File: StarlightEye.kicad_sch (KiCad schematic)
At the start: 96 parts, among them J1 QWIIC_CONNECTORJS-1MM, J2 FH12A-22S-0.5SH(55), J3 Conn_Coaxial, J4 Conn_Coaxial, J5 Conn_Coaxial, Q1 DMG2302UK-7, Q2 DMG2302UK-7, U1 AP3418KTR-G1, U2 LP5907MFX-1.8, U3 AP2161W, U4 IMX585, U5 ECS-2520MV-240-DN-TR

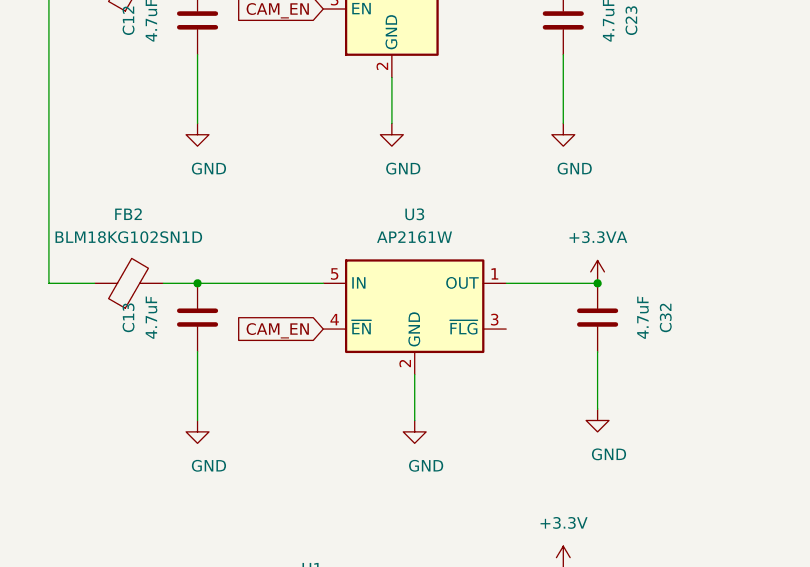
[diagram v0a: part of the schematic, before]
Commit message: Bug fix: swaping part no AP2161W with AP2171W to have the correct EN polarity
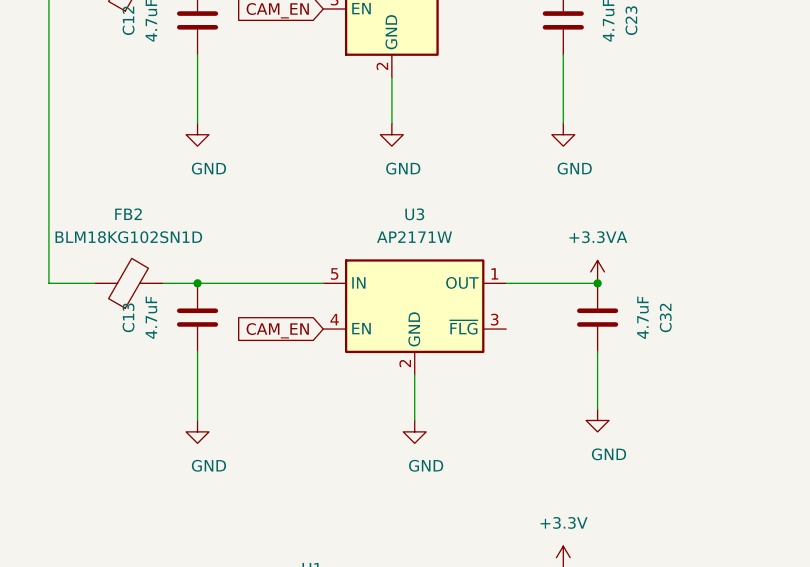
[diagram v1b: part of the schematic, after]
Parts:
- removed U3: AP2161W, Package_TO_SOT_SMD:SOT-23-5, symbol Power_Management:AP2161W
- added U3: AP2171W, Package_TO_SOT_SMD:SOT-23-5, symbol Power_Management:AP2171W
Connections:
- net +3.3VA: now also U3.1 (OUT)
- net CAM_EN: now also U3.4 (EN)
- net GND: now also U3.2 (GND)
- net at C13.2, FB2.2: now also U3.5 (IN)
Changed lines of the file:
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@@
     (pin "1")
+  )
+  (symbol (lib_id "Power_Management:AP2171W") (at 64.77 210.82 0) (unit 1)
+    (in_bom yes) (on_board yes) (fields_autoplaced)
+    (property "Reference" "U3" (id 0) (at 64.77 200.66 0))
+    (property "Value" "AP2171W" (id 1) (at 64.77 203.2 0))
+    (property "Footprint" "Package_TO_SOT_SMD:SOT-23-5" (id 2) (at 64.77 220.98 0)
+      (effects (font (size 1.27 1.27)) hide)
+    )
+    (property "Datasheet" "https://www.diodes.com/assets/Datasheets/AP2161.pdf" (id 3) (at 64.77 209.55 0)
+      (effects (font (size 1.27 1.27)) hide)
+    )
+    (pin "1")
+    (pin "2")
+    (pin "3")
+    (pin "4")
+    (pin "5")
   )
   (symbol (lib_id "power:+1V1") (at 92.71 107.95 0) (unit 1)
@@
     (pin "1")
     (pin "2")
-  )
-  (symbol (lib_id "Power_Management:AP2161W") (at 64.77 210.82 0) (unit 1)
-    (in_bom yes) (on_board yes) (fields_autoplaced)
-    (property "Reference" "U3" (id 0) (at 64.77 200.66 0))
-    (property "Value" "AP2161W" (id 1) (at 64.77 203.2 0))
-    (property "Footprint" "Package_TO_SOT_SMD:SOT-23-5" (id 2) (at 64.77 220.98 0)
-      (effects (font (size 1.27 1.27)) hide)
-    )
-    (property "Datasheet" "https://www.diodes.com/assets/Datasheets/AP2161.pdf" (id 3) (at 64.77 209.55 0)
-      (effects (font (size 1.27 1.27)) hide)
-    )
-    (pin "1")
-    (pin "2")
-    (pin "3")
-    (pin "4")
-    (pin "5")
   )
   (symbol (lib_id "power:GND") (at 39.37 43.18 0) (unit 1)
@@
       (reference "U2") (unit 1) (value "LP5907MFX-1.8") (footprint "Package_TO_SOT_SMD:SOT-23-5")
     )
-    (path "/b70f92fc-e7da-4598-aac3-42894166b45e"
-      (reference "U3") (unit 1) (value "AP2161W") (footprint "Package_TO_SOT_SMD:SOT-23-5")
+    (path "/2c71736d-9bd1-425e-bf48-2682b064493a"
+      (reference "U3") (unit 1) (value "AP2171W") (footprint "Package_TO_SOT_SMD:SOT-23-5")
     )
     (path "/b928e7ba-db52-4d1a-8842-81747bfca67f"

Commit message: V1.6 init
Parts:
- removed C13: 4.7uF, Capacitor_SMD:C_0603_1608Metric, symbol Device:C
- removed FB1, FB2: BLM18KG102SN1D, Inductor_SMD:L_0603_1608Metric, symbol Device:FerriteBead
- removed J1: QWIIC_CONNECTORJS-1MM, Connector_JST:JST_SH_SM04B-SRSS-TB_1x04-1MP_P1.00mm_Horizontal, symbol SparkFun-Connectors:QWIIC_CONNECTORJS-1MM
- removed Q1, Q2: DMG2302UK-7, Package_TO_SOT_SMD:SOT-23, symbol Transistor_FET:DMN30H4D0L
- removed TP5: TestPoint, TestPoint:TestPoint_Pad_D1.0mm, symbol Connector:TestPoint
- removed U3: AP2171W, Package_TO_SOT_SMD:SOT-23-5, symbol Power_Management:AP2171W
- added C13, C60: C_Feedthrough, footprints:NFM18CC101R1C3D, symbol Device:C_Feedthrough
- added C48, C51, C52, C53, C54, C55, C56: 100nF, Capacitor_SMD:C_0402_1005Metric, symbol Device:C
- added C49, C57: 10nF, Capacitor_SMD:C_0402_1005Metric, symbol Device:C
- added C50: 10uF, Capacitor_SMD:C_0603_1608Metric, symbol Device:C
- added C58: 100pF, Capacitor_SMD:C_0402_1005Metric, symbol Device:C
- added C59: 4.7uF, Capacitor_SMD:C_0603_1608Metric, symbol Device:C
- added C61: 120pF, Capacitor_SMD:C_0402_1005Metric, symbol Device:C
- added C62: 22uF, Capacitor_SMD:C_0805_2012Metric, symbol Device:C
- added D1: MBR0540, Diode_SMD:D_SOD-123, symbol Diode:MBR0540
- added FB4: BLM18KG102SN1D, Inductor_SMD:L_0402_1005Metric, symbol Device:FerriteBead
- added J1: Conn_01x04_Shielded, Connector_JST:JST_SH_SM04B-SRSS-TB_1x04-1MP_P1.00mm_Horizontal, symbol Connector_Generic_Shielded:Conn_01x04_Shielded
- added J6: Conn_01x02_Shielded, Connector_Molex:Molex_PicoBlade_53398-0271_1x02-1MP_P1.25mm_Vertical, symbol Connector_Generic_Shielded:Conn_01x02_Shielded
- added J7: Conn_01x02_Shielded, Connector_Molex:Molex_PicoBlade_53261-0271_1x02-1MP_P1.25mm_Horizontal, symbol Connector_Generic_Shielded:Conn_01x02_Shielded
- added R11, R13: 10K, Resistor_SMD:R_0402_1005Metric, symbol Device:R
- added R12: 1.15K, Resistor_SMD:R_0402_1005Metric, symbol Device:R
- added R14: 2K, Resistor_SMD:R_0402_1005Metric, symbol Device:R
- added TP14, TP7, TP_3V1: TestPoint, TestPoint:TestPoint_Pad_D1.0mm, symbol Connector:TestPoint
- added U10: TVS0500DRV, Package_SON:WSON-6-1EP_2x2mm_P0.65mm_EP1x1.6mm, symbol Power_Protection:TVS0500DRV
- added U11: TPSM82821SILR, footprints:TPSM82821SILR, symbol TPSM82821SILR:TPSM82821SILR
- added U3: TPS7A90, Package_DFN_QFN:Texas_S-PDSO-N10_EP1.2x2mm, symbol Regulator_Linear:TPS7A90
- added U6: TMP117AIDRVR, footprints:TMP117AIDRVR, symbol 2021-03-21_22-07-02:TMP117AIDRVR
- added U7: STM8S003F3P, Package_SO:TSSOP-20_4.4x6.5mm_P0.65mm, symbol MCU_ST_STM8:STM8S003F3P
- added U8: DRV8837C, Package_SON:WSON-8-1EP_2x2mm_P0.5mm_EP0.9x1.6mm, symbol Driver_Motor:DRV8837C
- added U9: TCA9406DC, footprints:TCA9406DCUR, symbol Interface:TCA9406DC
- C32: value 4.7uF -> 10uF
- R6: value 1K -> 10K
- R7: value 1K -> 3.57K
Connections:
- net +1V1: now also C58.2
- net +1V8: now also JP1.1 (A), JP2.1 (A), C55.1, U9.3 (VCCA), U9.6 (OE); no longer R4.2, R5.1, R6.2, R7.1
- net +3.3VA: now also R7.2, C50.1, C57.2, U3.1 (OUT), U3.2 (OUT); no longer C32.1
- net +3V3: now also C51.1, C53.1, C56.1, FB4.1, J1.2 (Pin_2), U7.9 (VDD), U8.8 (VCC), U9.7 (VCCB); no longer FB3.2
- net ADDR0: now also R5.1; no longer R5.2
- net CAM_EN: now also R6.1, U3.7 (EN)
- net GND: now also J2.MP, R4.2, R5.2, R6.2, C13.2, C48.1, C49.2, C50.2, C51.2, C52.1, C53.2, C54.2, C55.2, C56.2, C59.1, C60.2, C62.2, J1.1 (Pin_1), J1.MP (Shield), J6.MP (Shield), J7.2 (Pin_2), J7.MP (Shield), R11.2, R12.1, R14.1, U10.1 (GND), U10.2 (GND), U10.3 (GND), U10.7 (GND), U11.10 (GND), U11.9 (GND), U3.11 (GND), U3.4 (GND), U6.2 (GND), U6.3 (ALERT), U6.4 (ADD0), U7.7 (VSS), U8.4 (GND), U8.9 (GND), U9.2 (GND); no longer JP1.1 (A), JP2.1 (A)
- net SCL_1V8: now also U9.5 (SCL_A); no longer R6.1
- net SCL_3V3: now also J1.4 (Pin_4), U6.1 (SCL), U7.12 (PC2), U9.8 (SCL_B)
- net SDA_1V8: now also U9.4 (SDA_A); no longer R7.2
- net SDA_3V3: now also J1.3 (Pin_3), U6.6 (SDA), U7.11 (PC1), U9.1 (SDA_B)
- net at C12.2, U2.1 (IN): now also C13.1, C61.1, C62.1, R13.2, TP_3V1.1, U11.5 (VOUT), U11.6 (VOUT), U11.7 (VOUT)
- net at R1.2, R2.1, U1.5 (FB): now also C58.1
- new net: C60.1, D1.1 (K), U10.4 (IN), U10.5 (IN), U10.6 (IN)
- new net: C61.2, R13.1, R14.2, U11.8 (FB)
- new net: C57.1, R12.2, R7.1, U3.3 (FB)
- new net: C49.1, U3.8 (NR/SS)
- new net: C48.2, FB4.2, U6.5 (V+)
- new net: C13.3, C32.1, U3.10 (IN), U3.6 (SS_CTRL), U3.9 (IN)
- new net: J6.1 (Pin_1), U8.3 (OUT2)
- new net: J6.2 (Pin_2), U8.2 (OUT1)
- new net: D1.2 (A), J7.1 (Pin_1)
- new net +5V: C52.2, C59.2, C60.3, FB3.2, TP14.1, U11.1 (VIN), U11.2 (VIN), U11.3 (EN), U8.1 (VM)
- new net IN1: U7.2 (PD5), U8.6 (IN1)
- new net IN2: U7.3 (PD6), U8.5 (IN2)
- new net NRST: C54.1, U7.4 (NRST)
- new net SLEEP: R11.1, U7.1 (PD4), U8.7 (~{SLEEP})
- new net SWIO: TP7.1, U7.18 (PD1)
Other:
- note added: "Connectors"
- note added: "I2C ADDR: 0x48"
- note added: "I2C IR Filter Switch"
- note added: "I2C Level Shifter"
- note added: "IMX585"
- note added: "IMX585 Decoupling Caps"
- note added: "MISC"
- note added: "Power"
- note added: "Temperature Sensor"
- note added: "TestPoints"
- company: Will Whang -> WillWhang
- moved on the sheet: C1, C10, C11, C12, C14, C15, C16, C17, C18, C19, C2, C20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

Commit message: V1.7
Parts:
- added C63: 100n, Capacitor_SMD:C_0402_1005Metric, symbol Device:C
- added C64: 10nF, Capacitor_SMD:C_0402_1005Metric, symbol Device:C
- added C65: 2.2uF, Capacitor_SMD:C_0402_1005Metric, symbol Device:C
- added U12: ICM-42688-P, footprints:PQFN50P300X250X97-14N, symbol ICM-42688-P:ICM-42688-P
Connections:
- net +1V8: now also JP3.1 (A), C63.1, C64.1, C65.1, U12.12 (AP_CS), U12.5 (VDDIO), U12.8 (VDD); no longer R3.2
- net GND: now also R3.1, C63.2, C64.2, C65.2, U12.1 (AP_SDO/AP_AD0), U12.10 (RESV_10), U12.11 (RESV_11), U12.2 (RESV_2), U12.3 (RESV_3), U12.6 (GND), U12.7 (RESV_7); no longer JP3.1 (A)
- net SCL_1V8: now also U12.13 (AP_SCL/AP_SCLK)
- net SDA_1V8: now also U12.14 (AP_SDA/AP_SDIO/AP_SDI)
- net XMASTER: now also R3.2; no longer R3.1
- net XVS: now also U12.9 (INT2/FSYNC/CLKIN)
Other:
- note added: "I2C ADDR: 0x68"
- company: WillWhang -> (none)
- title: StarlightEye -> (none)
- moved on the sheet: C48, C55, C56, FB4, H1, H2, H3, H4, R3, R4, R5, R9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

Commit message: Ver 2.0 HW
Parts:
- removed C60: C_Feedthrough, footprints:NFM18CC101R1C3D, symbol Device:C_Feedthrough
- removed D1: MBR0540, Diode_SMD:D_SOD-123, symbol Diode:MBR0540
- removed J7: Conn_01x02_Shielded, Connector_Molex:Molex_PicoBlade_53261-0271_1x02-1MP_P1.25mm_Horizontal, symbol Connector_Generic_Shielded:Conn_01x02_Shielded
- removed TP11, TP12, TP14, TP6: TestPoint, TestPoint:TestPoint_Pad_D1.0mm, symbol Connector:TestPoint
- removed U10: TVS0500DRV, Package_SON:WSON-6-1EP_2x2mm_P0.65mm_EP1x1.6mm, symbol Power_Protection:TVS0500DRV
- removed U11: TPSM82821SILR, footprints:TPSM82821SILR, symbol TPSM82821SILR:TPSM82821SILR
- removed U12: ICM-42688-P, footprints:PQFN50P300X250X97-14N, symbol ICM-42688-P:ICM-42688-P
- added C60: 47uF, Capacitor_SMD:C_0603_1608Metric, symbol Device:C
- added C66: 10nF, Capacitor_SMD:C_0402_1005Metric, symbol Device:C
- added C67: 1uF, Capacitor_SMD:C_0402_1005Metric, symbol Device:C
- added R21, R22: DNP, Resistor_SMD:R_0402_1005Metric, symbol Device:R
- added TP5: TestPoint, TestPoint:TestPoint_Pad_D1.0mm, symbol Connector:TestPoint
- added U10: TPSM83100SIUR, footprints:MICROSIP8_SIU_TEX-L, symbol 2025-05-08_02-36-28:XTPSM83100SIUR
- added U11: ICM-42688-P, footprints:PQFN50P300X250X97-14N, symbol ICM-42688-P:ICM-42688-P
- C13: value C_Feedthrough -> NFM18PC104R1C3D
- C48: value 100nF -> 1uF
- C49: value 10nF -> 1uF
- C50: value 10uF -> 22uF
- C59: value 4.7uF -> 22uF
- C61: value 120pF -> 100pF
- C62: value 22uF -> 47uF; footprint Capacitor_SMD:C_0805_2012Metric -> Capacitor_SMD:C_0603_1608Metric
- C63: value 100n -> 22uF; footprint Capacitor_SMD:C_0402_1005Metric -> Capacitor_SMD:C_0603_1608Metric
- C64: value 10nF -> 10uF; footprint Capacitor_SMD:C_0402_1005Metric -> Capacitor_SMD:C_0603_1608Metric
- C65: value 2.2uF -> 100nF
- FL1, FL2, FL3, FL4, FL5: value DLP11SN900HL2L -> DLM0QSB120HY2D; footprint footprints:DLP11SA350HL2B -> footprints:DLM0QSB120HY2D
- J1: footprint Connector_JST:JST_SH_SM04B-SRSS-TB_1x04-1MP_P1.00mm_Horizontal -> Connector_JST:JST_SH_BM04B-SRSS-TB_1x04-1MP_P1.00mm_Vertical
- J2: value FH12A-22S-0.5SH(55) -> TF38-22S-0.5SV(830); footprint Connector_FFC-FPC:Hirose_FH12-22S-0.5SH_1x22-1MP_P0.50mm_Horizontal -> footprints:TF3822S05SV830
- J6: footprint Connector_Molex:Molex_PicoBlade_53398-0271_1x02-1MP_P1.25mm_Vertical -> Connector_Molex:Molex_PicoBlade_53261-0271_1x02-1MP_P1.25mm_Horizontal
- R10: value 22R -> DNP
- R13: value 10K -> 562K
- R14: value 2K -> 91K
- U5: value ECS-2520MV-240-DN-TR -> SX2M24.000M20F30TNN
- U7: value STM8S003F3P -> CH32V003F4P6
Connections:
- net +1V8: now also C66.1, C67.1, U11.12 (AP_CS), U11.5 (VDDIO), U11.8 (VDD); no longer C63.1, C64.1
- net +3V3: now also C59.2, C63.2, FB3.1, U10.1 (VIN), U10.7 (MODE), U10.8 (EN)
- net CLOCK: now also R10.2; no longer R10.1
- net GND: now also C63.1, C64.1, C60.2, C66.2, C67.2, TP5.1, U10.2 (GND), U10.3 (GND), U10.6 (GND), U11.1 (AP_SDO/AP_AD0), U11.10 (RESV_10), U11.11 (RESV_11), U11.2 (RESV_2), U11.3 (RESV_3), U11.6 (GND), U11.7 (RESV_7); no longer C63.2, C64.2
- net SCL_1V8: now also U9.4 (SDA_A), U11.13 (AP_SCL/AP_SCLK); no longer U9.5 (SCL_A)
- net SCL_3V3: now also U9.1 (SDA_B); no longer U9.8 (SCL_B)
- net SDA_1V8: now also U9.5 (SCL_A), U11.14 (AP_SDA/AP_SDIO/AP_SDI); no longer U9.4 (SDA_A)
- net SDA_3V3: now also U9.8 (SCL_B); no longer U9.1 (SDA_B)
- net XVS: now also U11.9 (INT2/FSYNC/CLKIN)
- net D0_N: now reaches FL1.2, J2.21 (Pin_21)
- net D0_P: now reaches FL1.3, J2.20 (Pin_20)
- net at C61.2, R13.1, R14.2: now also U10.5 (FB)
- net +3.6V: now reaches C12.2, C13.1, C61.1, C62.1, R13.2, TP_3V1.1, U2.1 (IN)
- net +3.6V: now also C52.2, C64.2, U8.1 (VM), C60.1, U10.4 (VOUT)
- net D1_N: now reaches FL2.2, J2.18 (Pin_18)
- net D1_P: now reaches FL2.3, J2.17 (Pin_17)
- net at J3.1 (In): now also R10.1; no longer R10.2
- net D3_N: now reaches FL5.2, J2.9 (Pin_9)
- net D3_P: now reaches FL5.3, J2.8 (Pin_8)
- net D2_P: now reaches FL4.3, J2.11 (Pin_11)
- net D2_N: now reaches FL4.2, J2.12 (Pin_12)
- net CLK_P: now reaches FL3.3, J2.14 (Pin_14)
- net CLK_N: now reaches FL3.2, J2.15 (Pin_15)
- net at C24.1, U1.4 (VIN): now also FB3.2; no longer FB3.1
- removed net +5V: C52.2, C59.2, FB3.2, U8.1 (VM)
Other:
- note added: "IMU"
- note added: "IMX585 Decoupling"
- note added: "Label"
- note removed: "IMX585 Decoupling Caps"
- company: (none) -> Will Whang
- title: (none) -> StarlightEye
- moved on the sheet: C12, C13, C22, C23, C24, C32, C36, C48, C49, C50, C51, C52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
